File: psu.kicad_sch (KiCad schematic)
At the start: 76 parts, among them J1 39-28-1243, J2 292161-3, J3 292161-3, J4 292161-3, J5 292161-3, J6 292161-3, Q1 IRLML6344TRPBF, Q2 BSS138, Q3 IRLML6344TRPBF, Q4 IRLML6344TRPBF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

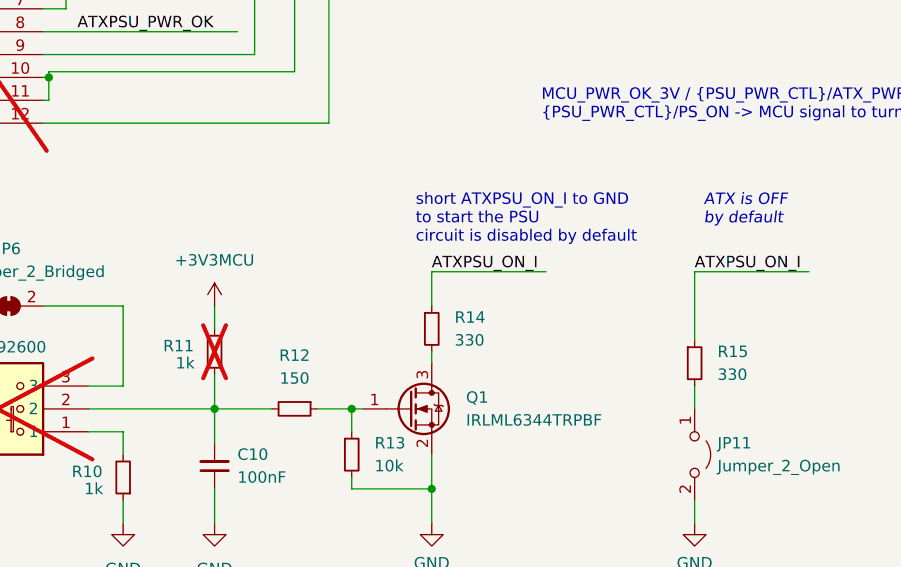
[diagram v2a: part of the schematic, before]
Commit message: pcb: R11 enables ATX on start
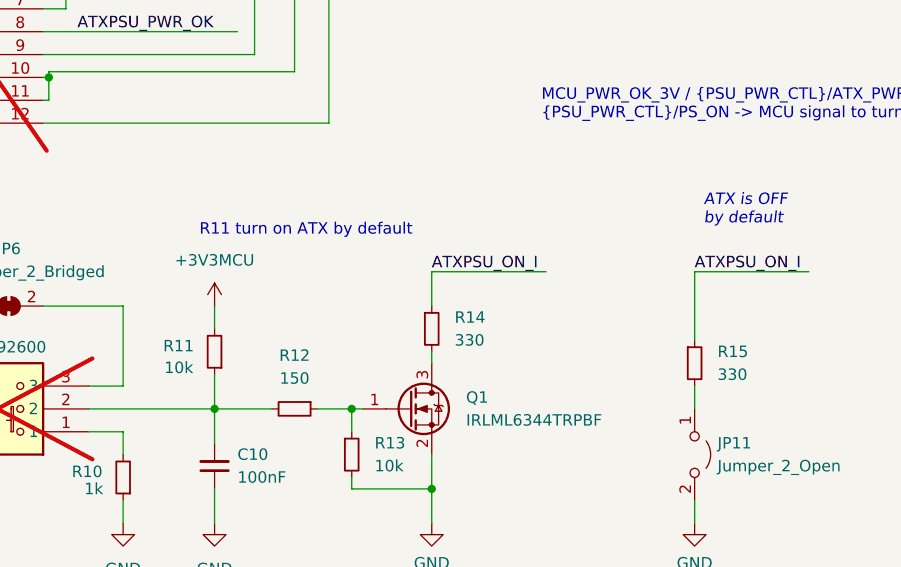
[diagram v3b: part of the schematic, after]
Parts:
- R11: value 1k -> 10k; JLCPCB Part # C11702 -> C25744; Part 0402WGF1001TCE -> 0402WGF1002TCE; now fitted
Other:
- note added: "R11 turn on ATX by default"
- note removed: "short ATXPSU_ON_I to GND to start the PSU circuit is disabled by default"
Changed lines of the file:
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@@
 		)
 	)
-	(text "short ATXPSU_ON_I to GND\nto start the PSU\ncircuit is disabled by default\n"
+	(text "R11 turn on ATX by default\n"
 		(exclude_from_sim no)
-		(at 102.362 65.532 0)
+		(at 90.17 64.008 0)
 		(effects
 			(font
 				(size 1.27 1.27)
 			)
-			(justify left bottom)
 		)
 	)
@@
 		(in_bom yes)
 		(on_board yes)
-		(dnp yes)
+		(dnp no)
 		(property "Reference" "R11"
 			(at 74.295 76.835 0)
@@
 			)
 		)
-		(property "Value" "1k"
-			(at 75.692 78.74 0)
+		(property "Value" "10k"
+			(at 74.422 79.248 0)
 			(effects
 				(font
@@
 			)
 		)
-		(property "JLCPCB Part #" "C11702"
+		(property "JLCPCB Part #" "C25744"
 			(at 80.01 77.47 0)
 			(effects
@@
 			)
 		)
-		(property "Part" "0402WGF1001TCE"
+		(property "Part" "0402WGF1002TCE"
 			(at 80.01 77.47 90)
 			(effects
